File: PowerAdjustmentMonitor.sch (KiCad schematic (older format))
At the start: 19 parts

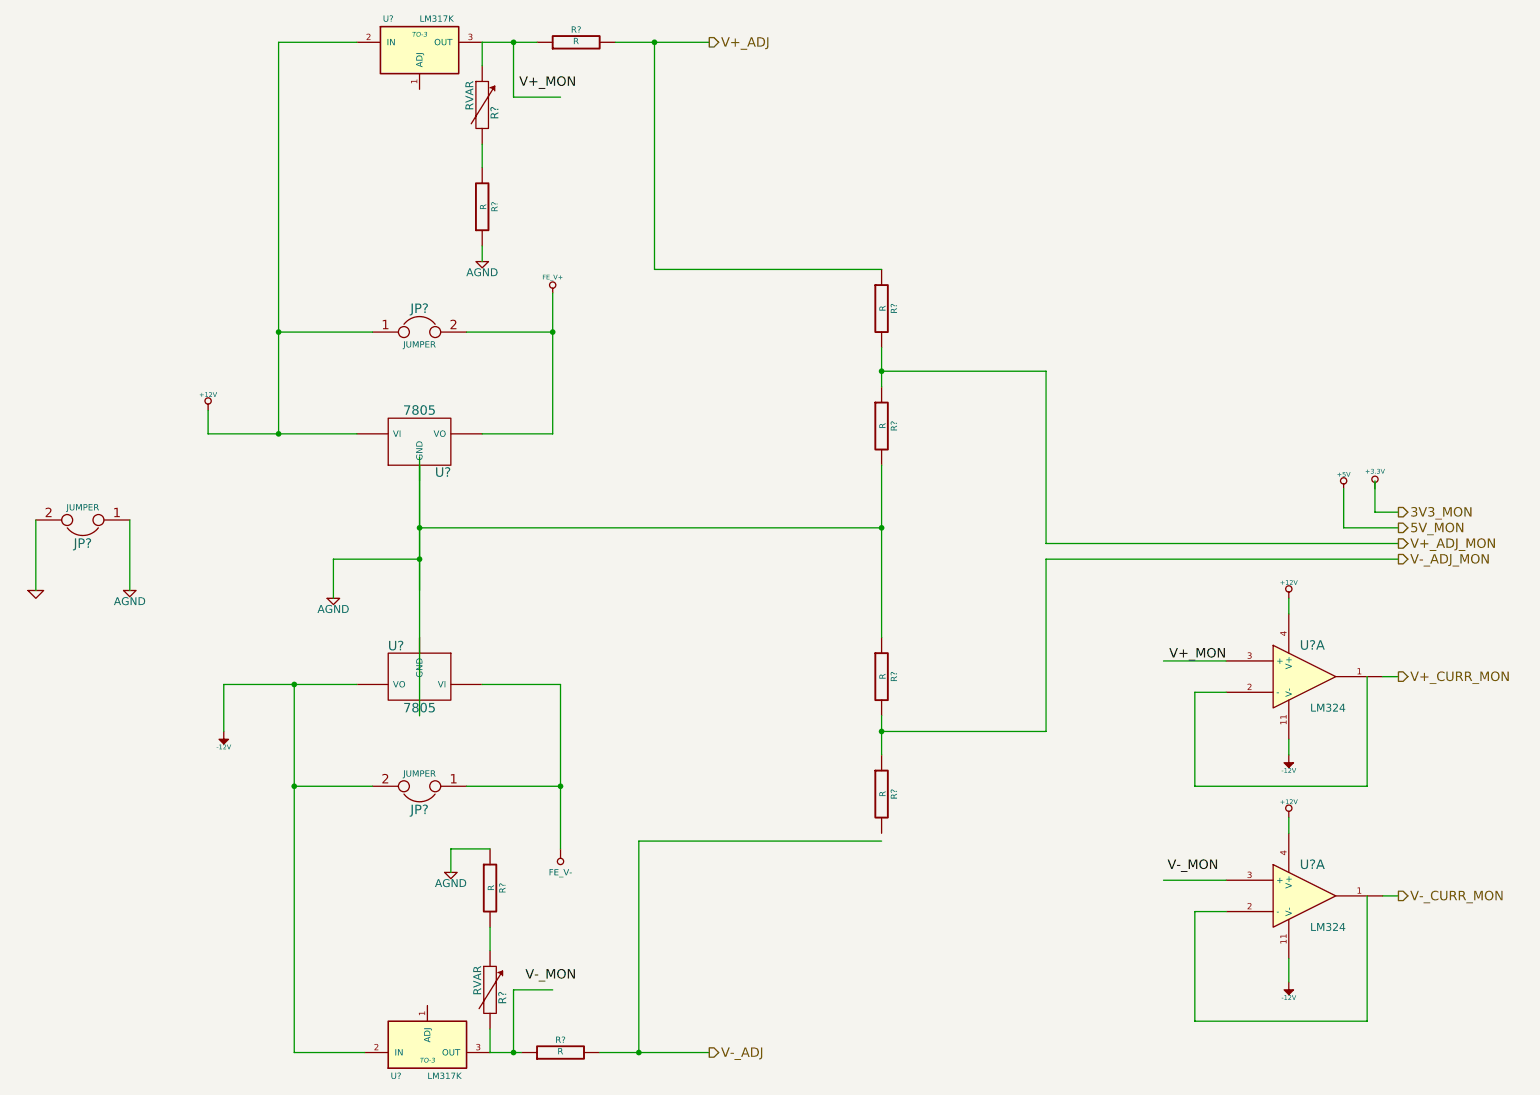
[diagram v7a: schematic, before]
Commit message: 5.3 Video 1/2 Associating and Placing the Relay Module
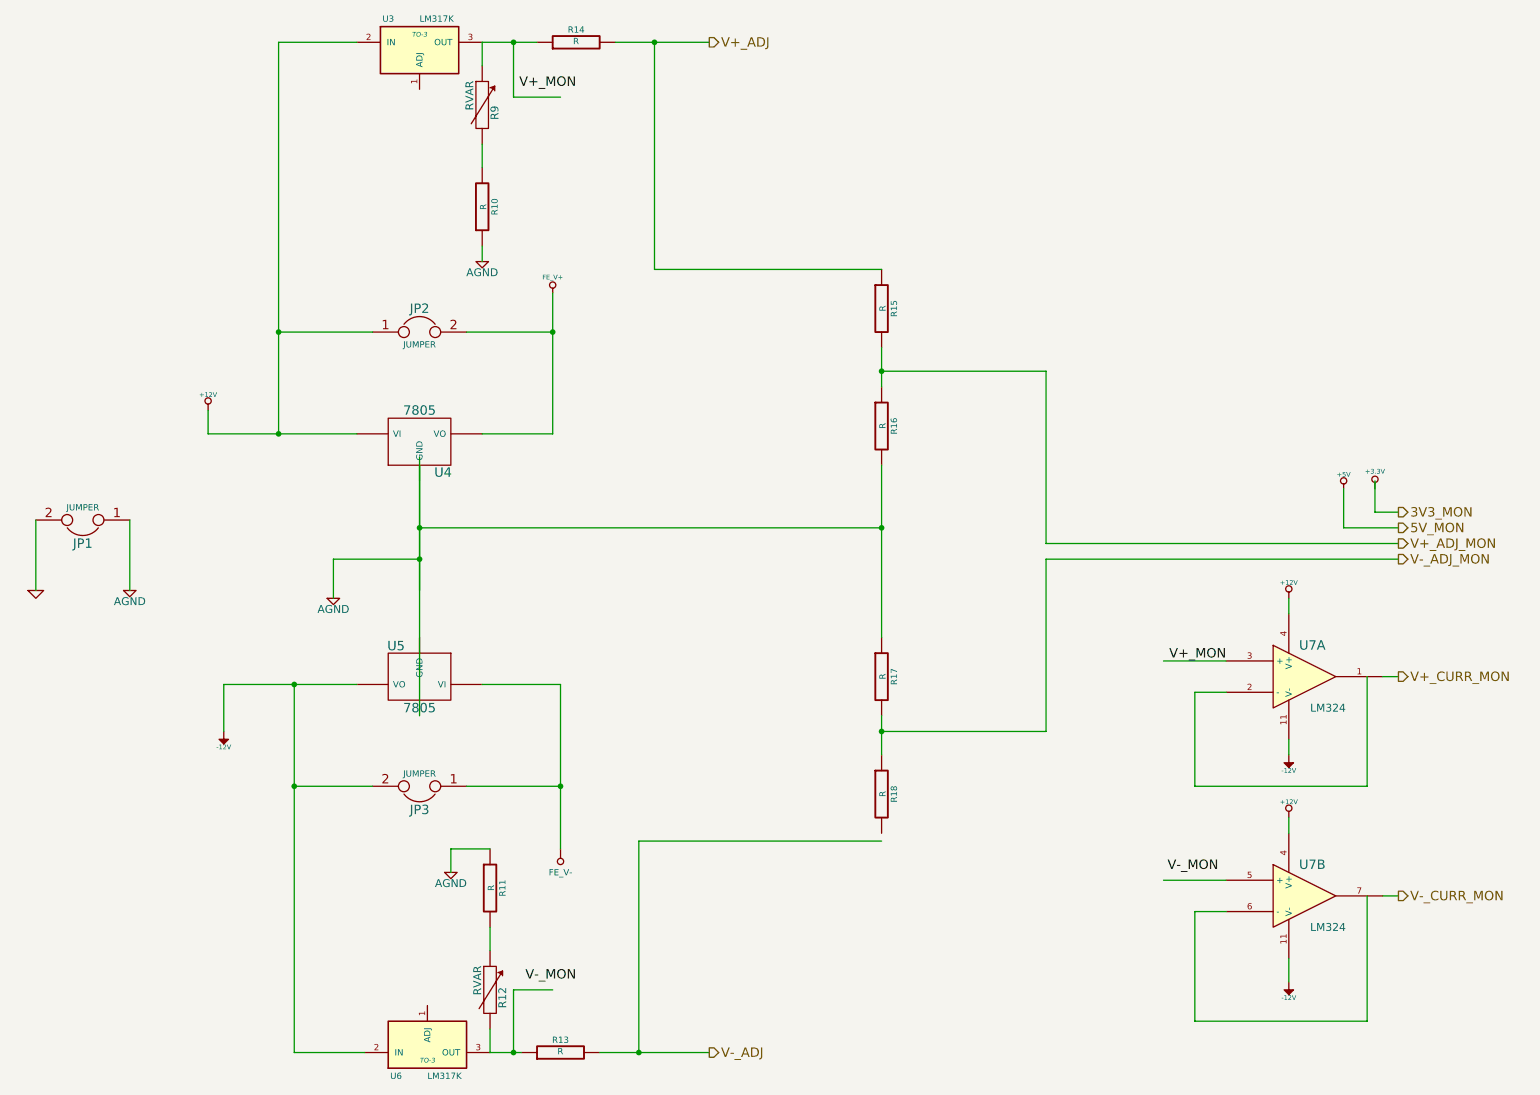
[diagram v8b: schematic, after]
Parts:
- gave numbers to parts that had none: 18
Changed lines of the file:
@@
 Sheet 9 9
 Title ""
-Date "10 feb 2014"
+Date "19 feb 2014"
 Rev ""
 Comp ""
@@
 $EndDescr
 $Comp
-L 7805 U?
+L 7805 U4
 U 1 1 52F50F52
 P 3850 3350
-F 0 "U?" H 4000 3154 60  0000 C CNN
+F 0 "U4" H 4000 3154 60  0000 C CNN
 F 1 "7805" H 3850 3550 60  0000 C CNN
 F 2 "" H 3850 3350 60  0000 C CNN
@@
 $EndComp
 $Comp
-L 7805 U?
+L 7805 U5
 U 1 1 52F50F5F
 P 3850 4850
-F 0 "U?" H 4000 4654 60  0000 C CNN
+F 0 "U5" H 4000 4654 60  0000 C CNN
 F 1 "7805" H 3850 5050 60  0000 C CNN
 F 2 "" H 3850 4850 60  0000 C CNN
@@
 $EndComp
 $Comp
-L R R?
+L R R11
 U 1 1 52F50F76
 P 4300 6200
-F 0 "R?" V 4380 6200 40  0000 C CNN
+F 0 "R11" V 4380 6200 40  0000 C CNN
 F 1 "R" V 4307 6201 40  0000 C CNN
 F 2 "" V 4230 6200 30  0000 C CNN
@@
 $EndComp
 $Comp
-L JUMPER JP?
+L JUMPER JP1
 U 1 1 52F50F85
 P 1700 3850
-F 0 "JP?" H 1700 4000 60  0000 C CNN
+F 0 "JP1" H 1700 4000 60  0000 C CNN
 F 1 "JUMPER" H 1700 3770 40  0000 C CNN
 F 2 "" H 1700 3850 60  0000 C CNN
@@
 $EndComp
 $Comp
-L JUMPER JP?
+L JUMPER JP2
 U 1 1 52F50F92
 P 3850 2650
-F 0 "JP?" H 3850 2800 60  0000 C CNN
+F 0 "JP2" H 3850 2800 60  0000 C CNN
 F 1 "JUMPER" H 3850 2570 40  0000 C CNN
 F 2 "" H 3850 2650 60  0000 C CNN
@@
 $EndComp
 $Comp
-L JUMPER JP?
+L JUMPER JP3
 U 1 1 52F50F98
 P 3850 5550
-F 0 "JP?" H 3850 5700 60  0000 C CNN
+F 0 "JP3" H 3850 5700 60  0000 C CNN
 F 1 "JUMPER" H 3850 5470 40  0000 C CNN
 F 2 "" H 3850 5550 60  0000 C CNN
@@
 $EndComp
 $Comp
-L GND #PWR?
+L GND #PWR020
 U 1 1 52F50FA0
 P 1400 4300
-F 0 "#PWR?" H 1400 4300 30  0001 C CNN
+F 0 "#PWR020" H 1400 4300 30  0001 C CNN
 F 1 "GND" H 1400 4230 30  0001 C CNN
 F 2 "" H 1400 4300 60  0000 C CNN
@@
 $EndComp
 $Comp
-L AGND #PWR?
+L AGND #PWR021
 U 1 1 52F50FB9
 P 2000 4300
-F 0 "#PWR?" H 2000 4300 40  0001 C CNN
+F 0 "#PWR021" H 2000 4300 40  0001 C CNN
 F 1 "AGND" H 2000 4230 50  0000 C CNN
 F 2 "" H 2000 4300 60  0000 C CNN
@@
 $EndComp
 $Comp
-L AGND #PWR?
+L AGND #PWR022
 U 1 1 52F50FF4
 P 3300 4350
-F 0 "#PWR?" H 3300 4350 40  0001 C CNN
+F 0 "#PWR022" H 3300 4350 40  0001 C CNN
 F 1 "AGND" H 3300 4280 50  0000 C CNN
 F 2 "" H 3300 4350 60  0000 C CNN
@@
 $EndComp
 $Comp
-L +12V #PWR?
+L +12V #PWR023
 U 1 1 52F5102D
 P 2500 3150
-F 0 "#PWR?" H 2500 3100 20  0001 C CNN
+F 0 "#PWR023" H 2500 3100 20  0001 C CNN
 F 1 "+12V" H 2500 3250 30  0000 C CNN
 F 2 "" H 2500 3150 60  0000 C CNN
@@
 $EndComp
 $Comp
-L -12V #PWR?
+L -12V #PWR024
 U 1 1 52F5104F
 P 2600 5200
-F 0 "#PWR?" H 2600 5330 20  0001 C CNN
+F 0 "#PWR024" H 2600 5330 20  0001 C CNN
 F 1 "-12V" H 2600 5300 30  0000 C CNN
 F 2 "" H 2600 5200 60  0000 C CNN
@@
 $EndComp
 $Comp
-L FE_V+ #PWR?
+L FE_V+ #PWR025
 U 1 1 52F5159F
 P 4700 2400
-F 0 "#PWR?" H 4700 2500 30  0001 C CNN
+F 0 "#PWR025" H 4700 2500 30  0001 C CNN
 F 1 "FE_V+" H 4700 2500 30  0000 C CNN
 F 2 "" H 4700 2400 60  0000 C CNN
@@
 $EndComp
 $Comp
-L FE_V- #PWR?
+L FE_V- #PWR28
 U 1 1 52F515C8
 P 4750 5950
-F 0 "#PWR?" H 4750 6150 40  0001 C CNN
+F 0 "#PWR28" H 4750 6150 40  0001 C CNN
 F 1 "FE_V-" H 4750 6100 40  0000 C CNN
 F 2 "" H 4750 5950 60  0000 C CNN
@@
 $EndComp
 $Comp
-L LM317K U?
+L LM317K U6
 U 1 1 52F51657
 P 3900 7200
-F 0 "U?" H 3700 7400 40  0000 C CNN
+F 0 "U6" H 3700 7400 40  0000 C CNN
 F 1 "LM317K" H 3900 7400 40  0000 L CNN
 F 2 "TO-3" H 3900 7300 30  0000 C CIN
@@
 $EndComp
 $Comp
-L AGND #PWR?
+L AGND #PWR026
 U 1 1 52F516D6
 P 4050 6100
-F 0 "#PWR?" H 4050 6100 40  0001 C CNN
+F 0 "#PWR026" H 4050 6100 40  0001 C CNN
 F 1 "AGND" H 4050 6030 50  0000 C CNN
 F 2 "" H 4050 6100 60  0000 C CNN
@@
 $EndComp
 $Comp
-L R R?
+L R R10
 U 1 1 52F51728
 P 4250 1850
-F 0 "R?" V 4330 1850 40  0000 C CNN
+F 0 "R10" V 4330 1850 40  0000 C CNN
 F 1 "R" V 4257 1851 40  0000 C CNN
 F 2 "" V 4180 1850 30  0000 C CNN
@@
 $EndComp
 $Comp
-L LM317K U?
+L LM317K U3
 U 1 1 52F5172F
 P 3850 850
-F 0 "U?" H 3650 1050 40  0000 C CNN
+F 0 "U3" H 3650 1050 40  0000 C CNN
 F 1 "LM317K" H 3850 1050 40  0000 L CNN
 F 2 "TO-3" H 3850 950 30  0000 C CIN
@@
 $EndComp
 $Comp
-L AGND #PWR?
+L AGND #PWR027
 U 1 1 52F51738
 P 4250 2200
-F 0 "#PWR?" H 4250 2200 40  0001 C CNN
+F 0 "#PWR027" H 4250 2200 40  0001 C CNN
 F 1 "AGND" H 4250 2130 50  0000 C CNN
 F 2 "" H 4250 2200 60  0000 C CNN
@@
 V-_ADJ
 $Comp
-L +3.3V #PWR?
+L +3.3V #PWR028
 U 1 1 52F517F0
 P 9950 3650
-F 0 "#PWR?" H 9950 3610 30  0001 C CNN
+F 0 "#PWR028" H 9950 3610 30  0001 C CNN
 F 1 "+3.3V" H 9950 3760 30  0000 C CNN
 F 2 "" H 9950 3650 60  0000 C CNN
@@
 V-_ADJ_MON
 $Comp
-L +5V #PWR?
+L +5V #PWR029
 U 1 1 52F51806
 P 9750 3650
-F 0 "#PWR?" H 9750 3740 20  0001 C CNN
+F 0 "#PWR029" H 9750 3740 20  0001 C CNN
 F 1 "+5V" H 9750 3740 30  0000 C CNN
 F 2 "" H 9750 3650 60  0000 C CNN
@@
 V-_CURR_MON
 $Comp
-L R R?
+L R R15
 U 1 1 52F5181A
 P 6800 2500
-F 0 "R?" V 6880 2500 40  0000 C CNN
+F 0 "R15" V 6880 2500 40  0000 C CNN
 F 1 "R" V 6807 2501 40  0000 C CNN
 F 2 "" V 6730 2500 30  0000 C CNN
@@
 $EndComp
 $Comp
-L R R?
+L R R16
 U 1 1 52F5182D
 P 6800 3250
-F 0 "R?" V 6880 3250 40  0000 C CNN
+F 0 "R16" V 6880 3250 40  0000 C CNN
 F 1 "R" V 6807 3251 40  0000 C CNN
 F 2 "" V 6730 3250 30  0000 C CNN
@@
 	6800 2750 6800 3000
 $Comp
-L R R?
+L R R17
 U 1 1 52F51905
 P 6800 4850
-F 0 "R?" V 6880 4850 40  0000 C CNN
+F 0 "R17" V 6880 4850 40  0000 C CNN
 F 1 "R" V 6807 4851 40  0000 C CNN
 F 2 "" V 6730 4850 30  0000 C CNN
@@
 $EndComp
 $Comp
-L R R?
+L R R18
 U 1 1 52F5190B
 P 6800 5600
-F 0 "R?" V 6880 5600 40  0000 C CNN
+F 0 "R18" V 6880 5600 40  0000 C CNN
 F 1 "R" V 6807 5601 40  0000 C CNN
 F 2 "" V 6730 5600 30  0000 C CNN
@@
 	9750 3900 10100 3900
 $Comp
-L R R?
+L R R13
 U 1 1 52F51ABE
 P 4750 7250
-F 0 "R?" V 4830 7250 40  0000 C CNN
+F 0 "R13" V 4830 7250 40  0000 C CNN
 F 1 "R" V 4757 7251 40  0000 C CNN
 F 2 "" V 4680 7250 30  0000 C CNN
@@
 	4300 7250 4500 7250
 $Comp
-L R R?
+L R R14
 U 1 1 52F51B5C
 P 4850 800
-F 0 "R?" V 4930 800 40  0000 C CNN
+F 0 "R14" V 4930 800 40  0000 C CNN
 F 1 "R" V 4857 801 40  0000 C CNN
 F 2 "" V 4780 800 30  0000 C CNN
@@
 V+_MON
 $Comp
-L LM324 U?
+L LM324 U7
 U 1 1 52F51E74
 P 9500 4850
-F 0 "U?" H 9550 5050 60  0000 C CNN
+F 0 "U7" H 9550 5050 60  0000 C CNN
 F 1 "LM324" H 9650 4650 50  0000 C CNN
 F 2 "" H 9500 4850 60  0000 C CNN
@@
 $EndComp
 $Comp
-L LM324 U?
-U 1 1 52F51E7A
+L LM324 U7
+U 2 1 52F51E7A
 P 9500 6250
-F 0 "U?" H 9550 6450 60  0000 C CNN
+F 0 "U7" H 9550 6450 60  0000 C CNN
 F 1 "LM324" H 9650 6050 50  0000 C CNN
 F 2 "" H 9500 6250 60  0000 C CNN
 F 3 "" H 9500 6250 60  0000 C CNN
-	1    9500 6250
+	2    9500 6250
 	1    0    0    -1
 $EndComp
@@
 	10000 6250 10100 6250
 $Comp
-L +12V #PWR?
+L +12V #PWR030
 U 1 1 52F51F5F
 P 9400 4350
-F 0 "#PWR?" H 9400 4300 20  0001 C CNN
+F 0 "#PWR030" H 9400 4300 20  0001 C CNN
 F 1 "+12V" H 9400 4450 30  0000 C CNN
 F 2 "" H 9400 4350 60  0000 C CNN
@@
 	9400 4350 9400 4450
 $Comp
-L +12V #PWR?
+L +12V #PWR031
 U 1 1 52F51FC1
 P 9400 5750
-F 0 "#PWR?" H 9400 5700 20  0001 C CNN
+F 0 "#PWR031" H 9400 5700 20  0001 C CNN
 F 1 "+12V" H 9400 5850 30  0000 C CNN
 F 2 "" H 9400 5750 60  0000 C CNN
@@
 	9400 5750 9400 5850
 $Comp
-L -12V #PWR?
+L -12V #PWR032
 U 1 1 52F5201F
 P 9400 5350
-F 0 "#PWR?" H 9400 5480 20  0001 C CNN
+F 0 "#PWR032" H 9400 5480 20  0001 C CNN
 F 1 "-12V" H 9400 5450 30  0000 C CNN
 F 2 "" H 9400 5350 60  0000 C CNN
@@
 	9400 5250 9400 5350
 $Comp
-L -12V #PWR?
+L -12V #PWR033
 U 1 1 52F5207B
 P 9400 6800
-F 0 "#PWR?" H 9400 6930 20  0001 C CNN
+F 0 "#PWR033" H 9400 6930 20  0001 C CNN
 F 1 "-12V" H 9400 6900 30  0000 C CNN
 F 2 "" H 9400 6800 60  0000 C CNN
@@
 V-_MON
 $Comp
-L RVAR R?
+L RVAR R12
 U 1 1 52F526E6
 P 4300 6850
-F 0 "R?" V 4380 6800 50  0000 C CNN
+F 0 "R12" V 4380 6800 50  0000 C CNN
 F 1 "RVAR" V 4220 6910 50  0000 C CNN
 F 2 "" H 4300 6850 60  0000 C CNN
@@
 $EndComp
 $Comp
-L RVAR R?
+L RVAR R9
 U 1 1 52F526F3
 P 4250 1200
-F 0 "R?" V 4330 1150 50  0000 C CNN
+F 0 "R9" V 4330 1150 50  0000 C CNN
 F 1 "RVAR" V 4170 1260 50  0000 C CNN
 F 2 "" H 4250 1200 60  0000 C CNN
